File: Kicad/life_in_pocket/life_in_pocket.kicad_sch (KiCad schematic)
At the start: 6 parts, among them J1 USB Breakout module, J6 Charging module, U1 ESP32-S3-WROOM-1, U2 Adafruit I2S 3W Class D Ampli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

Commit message: First push
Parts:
- removed J1: USB Breakout module, USB Breakout board:Usb_breakout board, symbol Connector_Generic:Conn_01x08
- removed J6: Charging module, Charging module:TP4056-Module, symbol Connector_Generic:Conn_01x06
- added BT1: Battery_Cell, Connector_JST:JST_PH_B2B-PH-K_1x02_P2.00mm_Vertical, symbol Device:Battery_Cell
- added C1, C2, C3: 4.7uF, Capacitor_SMD:C_0603_1608Metric, symbol PCM_SparkFun-Capacitor:4.7uF_0402_6.3V_10%
- added C10, C11, C13, C14: 0.1uF, Capacitor_SMD:C_0603_1608Metric, symbol PCM_SparkFun-Capacitor:0.1uF_0402_16V_10%
- added C12: 100nf, Capacitor_SMD:C_0603_1608Metric, symbol PCM_SparkFun-Capacitor:C
- added C15: 10uf, Capacitor_SMD:C_0603_1608Metric, symbol PCM_SparkFun-Capacitor:C
- added C4: 100nf, Capacitor_SMD:C_0603_1608Metric, symbol PCM_SparkFun-Capacitor:0.1uF_0402_16V_10%
- added C5, C6, C7: 22 µF, Capacitor_SMD:C_0603_1608Metric, symbol Device:C
- added C8, C9: 10 µF, Capacitor_SMD:C_0603_1608Metric, symbol Device:C
- added D1: LED, LED_SMD:LED_0603_1608Metric, symbol PCM_SparkFun-LED:LED
- added D2: S2JTR, Diode_SMD:D_0603_1608Metric, symbol Diode:S2JTR
- added D3: Green, LED_SMD:LED_0603_1608Metric, symbol PCM_SparkFun-LED:LED_Green_1206
- added D4: Blue, LED_SMD:LED_0603_1608Metric, symbol PCM_SparkFun-LED:LED_Green_1206
- added D5: Red, LED_SMD:LED_0603_1608Metric, symbol PCM_SparkFun-LED:LED_Green_1206
- added DS1: 2inch TFT, 2inch tft Adafruit:MODULE_4311, symbol Tft 2inch adafruit:4311
- added J2: USB_C_Receptacle_USB2.0_16P, Connector_USB:USB_C_Receptacle_GCT_USB4105-xx-A_16P_TopMnt_Horizontal, symbol Connector:USB_C_Receptacle_USB2.0_16P
- added L1: 1.5 µH, Inductor_SMD:L_0603_1608Metric, symbol Device:L_Small
- added Q1: QM6015D, Package_TO_SOT_SMD:TO-252-2, symbol Transistor_FET:QM6015D
- added R1: 470, Resistor_SMD:R_0603_1608Metric, symbol PCM_SparkFun-Resistor:1M_0402
- added R10, R11, R12: 330, Resistor_SMD:R_0603_1608Metric, symbol PCM_SparkFun-Resistor:3.3k_0402
- added R13: 33, Resistor_SMD:R_0603_1608Metric, symbol PCM_SparkFun-Resistor:330_0603
- added R14, R15: 10k, Resistor_SMD:R_0603_1608Metric, symbol PCM_SparkFun-Resistor:1k_0402
- added R16: 2k, Resistor_SMD:R_0603_1608Metric, symbol PCM_SparkFun-Resistor:1M_0402
- added R17, R2: 1k, Resistor_SMD:R_0603_1608Metric, symbol PCM_SparkFun-Resistor:3.3k_0402
- added R3, R4, R8: 5.1k, Resistor_SMD:R_0603_1608Metric, symbol PCM_SparkFun-Resistor:5.1k_0402
- added R5, R6, R7: 1M, Resistor_SMD:R_0603_1608Metric, symbol PCM_SparkFun-Resistor:1M_0402
- added R9: 10k, Resistor_SMD:R_0603_1608Metric, symbol PCM_SparkFun-Resistor:10k_4x0603_Array
- added SW1: SW_SPST, Connector_Wire:SolderWire-1sqmm_1x02_P7.8mm_D1.4mm_OD3.9mm, symbol Switch:SW_SPST
- added SW2, SW3: Switch, Button_Switch_SMD:SW_Push_1P1T_NO_CK_KSC6xxG, symbol ScottoKeebs:Placeholder_Switch
- added SW4, SW5: Switch, ScottoKeebs_MX:MX_PCB_1.00u, symbol ScottoKeebs:Placeholder_Switch
- added U3: MicroSd breakout, MicroSd breakout Adafruit:MODULE_MICROSD_SPI_OR_SDIO_CARD, symbol Mcrosd breakout adafruit 3.3v:MICROSD_SPI_OR_SDIO_CARD
- added U4: MCP73831, PCM_SparkFun-Semiconductor-Standard:SOT23-5, symbol PCM_SparkFun-IC-Power:MCP73831
- added U5: TPS63020, TPS63020:QFN14_1, symbol TPS63020:TPS63020
- added U6: MCP23017_SP, Package_DIP:DIP-28_W7.62mm, symbol Interface_Expansion:MCP23017_SP
- added U7, U8: TTP223, TTP223:MODULE_ZC440600, symbol TTP223 module:ZC440600
- Cam_module1: footprint (none) -> Connector_PinHeader_2.54mm:PinHeader_2x09_P2.54mm_Vertical
- M1: footprint (none) -> INMP441_Microphone:INMP441_module
- U2: footprint (none) -> MAX98357A_custom:MAX98357A_Adafruit_Breakout
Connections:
- net GND: now reaches Cam_module1.1 (GND)
- net GND: now also M1.GND, M1.L/R, U1.1 (GND), U1.40 (GND), U1.41 (GND), U2.6 (GND), BT1.2 (-), C1.1, C10.2, C11.1, C12.2, C13.2, C14.2, C15.2, C2.1, C3.2, C4.2, C5.2, C6.2, C7.2, C8.2, C9.2, D3.1 (K), D4.1 (K), D5.1 (K), DS1.7 (GND), J2.A1 (GND), J2.A12 (GND), J2.B1 (GND), J2.B12 (GND), J2.S1 (SHIELD), R14.1, R15.1, R16.1, R3.2, R4.2, R6.1, R8.1, SW2.2, SW3.2, U3.2 (GND), U4.2 (GND), U5.P2 (GND), U5.PAD (PGND), U6.10 (VSS), U6.15 (A0), U6.16 (A1), U6.17 (A2), U7.3 (GND), U8.3 (GND)
- net 3.3V: now reaches Cam_module1.10 (3.3v)
- net 3.3V: now also M1.VDD, U1.2 (3V3), U1.27 (GPIO0/BOOT), U1.3 (EN), U2.7 (V+), C10.1, C11.2, C12.1, C13.1, C14.1, C15.1, C5.1, C6.1, C7.1, DS1.6 (VCC), R14.2, R15.2, R17.2, R2.2, R5.2, R7.2, R9.1, SW2.1, SW3.1, U3.1 (3V), U5.P4 (VOUT), U5.P5 (VOUT), U6.9 (VDD), U7.2 (VCC), U8.2 (VCC)
- net CAM_VS: now reaches Cam_module1.11 (VS)
- net CAM_VS: now also U1.6 (GPIO6/TOUCH6/ADC1_CH5)
- net CAM_HS: now reaches Cam_module1.12 (HS)
- net CAM_HS: now also U1.7 (GPIO7/TOUCH7/ADC1_CH6)
- net CAM_RST: now reaches Cam_module1.13 (RST)
- net CAM_RST: now also U6.22 (GPA1)
- net D1: now reaches Cam_module1.14 (D1)
- net D1: now also U1.22 (GPIO14/TOUCH14/ADC2_CH3/FSPIWP/FSPIDQS/SUBSPIWP)
- net D3: now reaches Cam_module1.15 (D3)
- net D3: now also U1.9 (GPIO16/U0CTS/ADC2_CH5/XTAL_32K_N)
- net D5: now reaches Cam_module1.16 (D5)
- net D5: now also U1.15 (GPIO3/TOUCH3/ADC1_CH2)
- net CAM_SCL: now reaches Cam_module1.2 (SCL)
- net CAM_SCL: now also U1.12 (GPIO8/TOUCH8/ADC1_CH7/SUBSPICS1), U6.12 (SCK)
- net CAM_SDA: now reaches Cam_module1.3 (SDA)
- net CAM_SDA: now also U1.17 (GPIO9/TOUCH9/ADC1_CH8/FSPIHD/SUBSPIHD), U6.13 (SDA)
- net D0: now reaches Cam_module1.4 (DO)
- net D0: now also U1.26 (GPIO45)
- net D2: now reaches Cam_module1.5 (D2)
- net D2: now also U1.24 (GPIO47/SPICLK_P/SUBSPICLK_P_DIFF)
- net D4: now reaches Cam_module1.6 (D4)
- net D4: now also U1.23 (GPIO21)
- net D6: now reaches Cam_module1.7 (D6)
- net D6: now also U1.16 (GPIO46)
- net PCKL: now reaches Cam_module1.8 (PCKL)
- net PCKL: now also U1.21 (GPIO13/TOUCH13/ADC2_CH2/FSPIQ/FSPIIO7/SUBSPIQ)
- net PWDN: now reaches Cam_module1.9 (PWDN)
- net PWDN: now also U6.24 (GPA3)
- net MIC_SCK: now reaches M1.SCK
- net MIC_SCK: now also U1.34 (MTDI/GPIO41/CLK_OUT1), U2.2 (BClk)
- net MIC_SD: now reaches M1.SD
- net MIC_SD: now also U1.38 (GPIO2/TOUCH2/ADC1_CH1)
- net MIC_WS: now reaches M1.WS
- net MIC_WS: now also U1.35 (MTMS/GPIO42), U2.1 (LRClk)
- net SD D3/CS: now reaches U1.10 (GPIO17/U1TXD/ADC2_CH6)
- net SD D3/CS: now also U3.6 (D3/CS)
- net INT_B: now reaches U1.11 (GPIO18/U1RXD/ADC2_CH7/CLK_OUT3)
- net INT_B: now also U6.19 (INTB)
- net D-: now reaches U1.13 (GPIO19/U1RTS/ADC2_CH8/CLK_OUT2/USB_D-)
- net D-: now also J2.A6 (D+), J2.B6 (D+)
- net D+: now reaches U1.14 (GPIO20/U1CTS/ADC2_CH9/CLK_OUT1/USB_D+)
- net D+: now also J2.A7 (D-), J2.B7 (D-)
- net SD_CLK: now reaches U1.18 (GPIO10/TOUCH10/ADC1_CH9/FSPICS0/FSPIIO4/SUBSPICS0)
- net SD_CLK: now also U3.3 (CLK)
- net SD_CMD/SI: now reaches U1.19 (GPIO11/TOUCH11/ADC2_CH0/FSPID/FSPIIO5/SUBSPID)
- net SD_CMD/SI: now also U3.5 (CMD/SI)
- net SD_D0: now reaches U1.20 (GPIO12/TOUCH12/ADC2_CH1/FSPICLK/FSPIIO6/SUBSPICLK)
- net SD_D0: now also U3.4 (D0/SO)
- net at U1.32 (MTCK/GPIO39/CLK_OUT3/SUBSPICS1): now also R13.2
- net TFT_SDA: now reaches U1.33 (MTDO/GPIO40/CLK_OUT2)
- net TFT_SDA: now also DS1.4 (SDA)
- net TFT_CS: now reaches U1.39 (GPIO1/TOUCH1/ADC1_CH0)
- net TFT_CS: now also DS1.1 (CS)
- net AMP_DIN: now reaches U1.4 (GPIO4/TOUCH4/ADC1_CH3)
- net AMP_DIN: now also U2.3 (Din)
- net D7: now reaches U1.5 (GPIO5/TOUCH5/ADC1_CH4)
- net D7: now also Cam_module1.17 (D7)
- net TFT_DC: now reaches U1.8 (GPIO15/U0RTS/ADC2_CH4/XTAL_32K_P)
- net TFT_DC: now also DS1.2 (DC)
- new net: D1.1 (K), R1.2
- new net: U6.4 (GPB3), U7.1 (SIG)
- new net: C8.1, C9.1, D2.2 (A), Q1.1 (G), Q1.3 (S), R8.2, U5.P10 (VIN), U5.P11 (VIN)
- new net: SW5.1, U6.8 (GPB7)
- new net: R17.1, SW5.2
- new net: R1.1, U4.1 (STAT)
- new net: R16.2, U4.5 (PROG)
- new net: U6.6 (GPB5), U8.1 (SIG)
- new net: BT1.1 (+), SW1.1 (A)
- new net: J2.B5 (CC2), R4.1
- new net: R10.1, U6.1 (GPB0)
- new net: D3.2 (A), R10.2
- new net: R11.1, U6.2 (GPB1)
- new net: D4.2 (A), R11.2
- new net: R2.1, SW4.2
- new net: R9.2, U6.18 (~{RESET})
- new net: R12.1, U6.3 (GPB2)
- new net: SW4.1, U6.7 (GPB6)
- new net: J2.A5 (CC1), R3.1
- new net: C4.1, U5.P1 (VINA), U5.P12 (EN), U5.P13 (PS/SYNC)
- new net: R5.1, R6.2, U5.P3 (FB)
- new net: L1.2, U5.P6 (L2), U5.P7 (L2)
- new net: L1.1, U5.P8 (L1), U5.P9 (L1)
- new net: D5.2 (A), R12.2
- new net AMP_SD: U2.5 (SD_Mode), U6.21 (GPA0)
- new net BAT+: C1.2, C2.2, Q1.2 (D), SW1.2 (B), U4.3 (V_{BAT})
- new net GPA7: R7.1, U5.P14 (PG), U6.28 (GPA7)
- new net TFT_RST: DS1.3 (RST), U6.23 (GPA2)
- new net TFT_SCL: DS1.5 (SCL), R13.1
- new net VBUS: C3.1, D1.2 (A), D2.1 (K), J2.A4 (VBUS), J2.A9 (VBUS), J2.B4 (VBUS), J2.B9 (VBUS), U4.4 (VIN)
- no-connect marks 0 -> 13
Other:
- moved on the sheet: Cam_module1, M1, U2

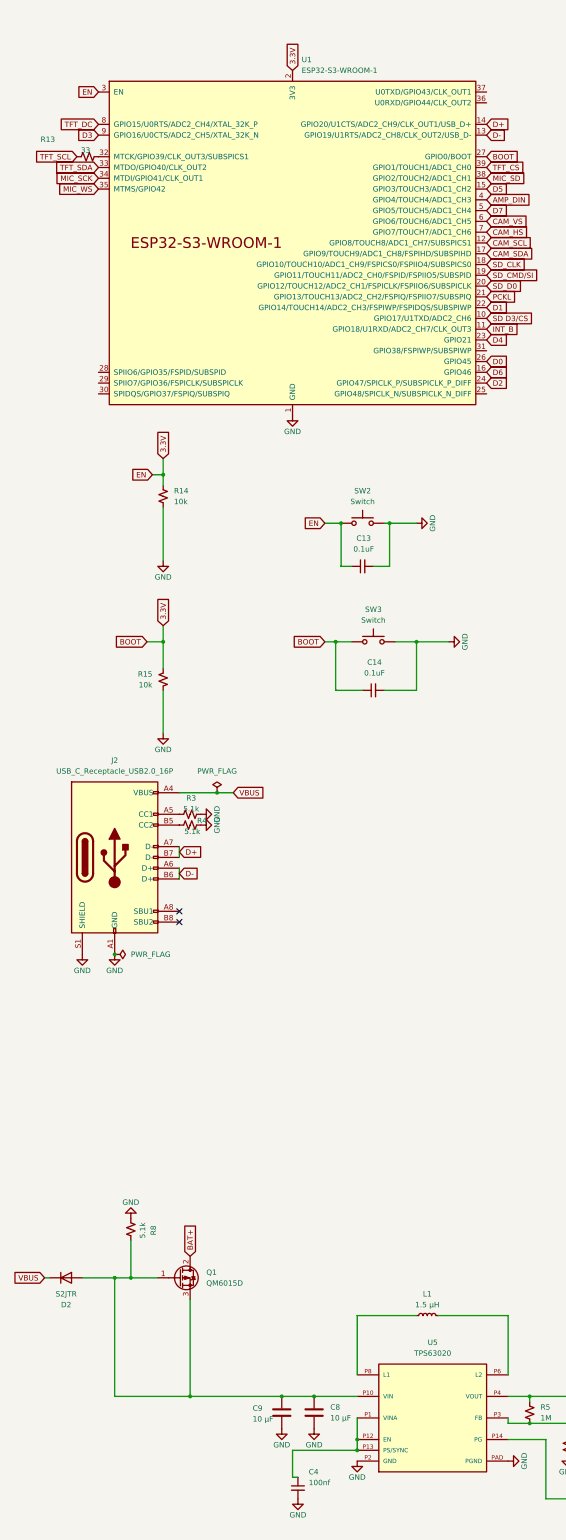
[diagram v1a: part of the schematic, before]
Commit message: Finished rerouting- all critical errors resolved
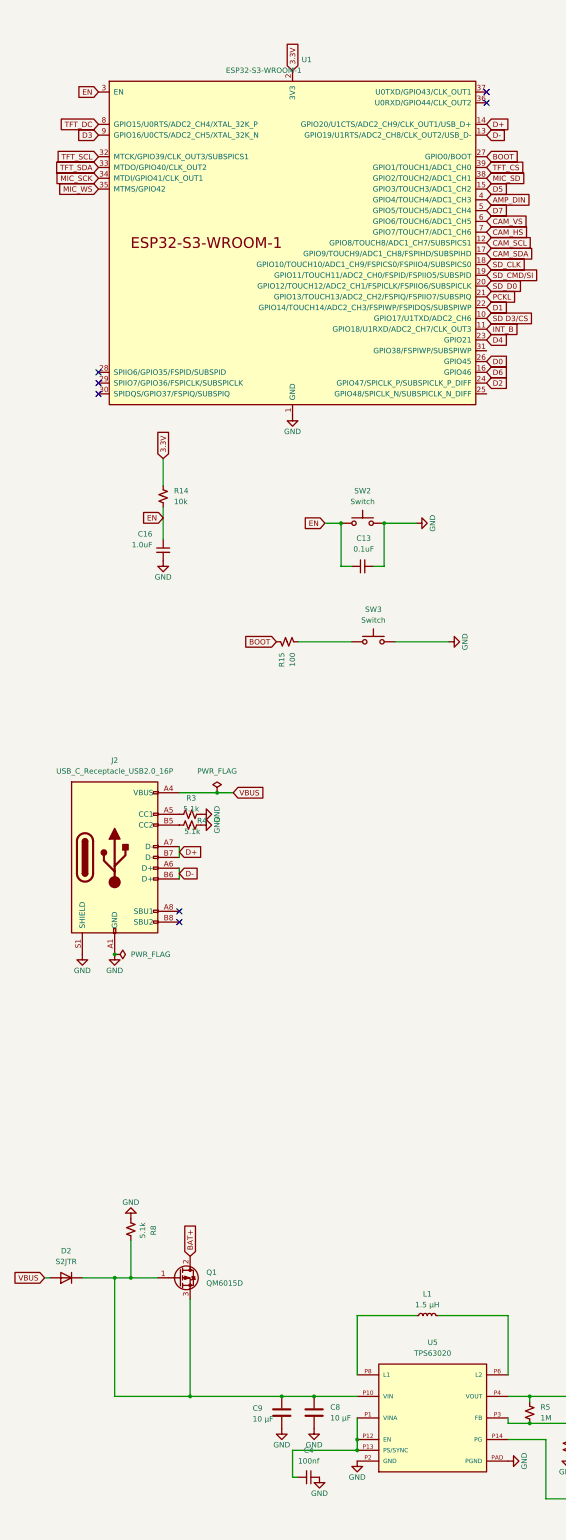
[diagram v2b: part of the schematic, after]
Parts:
- removed C14: 0.1uF, Capacitor_SMD:C_0603_1608Metric, symbol PCM_SparkFun-Capacitor:0.1uF_0402_16V_10%
- removed R13: 33, Resistor_SMD:R_0603_1608Metric, symbol PCM_SparkFun-Resistor:330_0603
- added C16: 1.0uF, Capacitor_SMD:C_0603_1608Metric, symbol PCM_SparkFun-Capacitor:1.0uF_0402_16V_10%
- R15: value 10k -> 100
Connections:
- net 3.3V: no longer C13.1, R15.2, SW2.1, SW3.1, U1.27 (GPIO0/BOOT), U1.3 (EN)
- net GND: now also C4.1, C16.2; no longer C4.2, R14.1, R15.1
- net TFT_SCL: now also U1.32 (MTCK/GPIO39/CLK_OUT3/SUBSPICS1)
- net VBUS: now also D2.2 (A); no longer D2.1 (K)
- net at C8.1, C9.1, Q1.1 (G)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: now also D2.1 (K); no longer D2.2 (A)
- net at U5.P1 (VINA), U5.P12 (EN), U5.P13 (PS/SYNC): now also C4.2; no longer C4.1
- new net: R15.1, SW3.1
- new net BOOT: R15.2, U1.27 (GPIO0/BOOT)
- new net EN: C13.1, C16.1, R14.1, SW2.1, U1.3 (EN)
- no-connect marks 13 -> 18
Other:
- moved on the sheet: C4, D2, R15

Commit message: Kicad stuff done. began firmware setup
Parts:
- added H1, H2, H3, H4: MountingHole_Pad, MountingHole:MountingHole_3.2mm_M3, symbol Mechanical:MountingHole_Pad
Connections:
- net GND: now also H1.1, H2.1, H3.1, H4.1
- no-connect marks 18 -> 17
